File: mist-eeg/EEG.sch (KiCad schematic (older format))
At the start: 62 parts, among them J3 Electrodes, U8 ADS1299

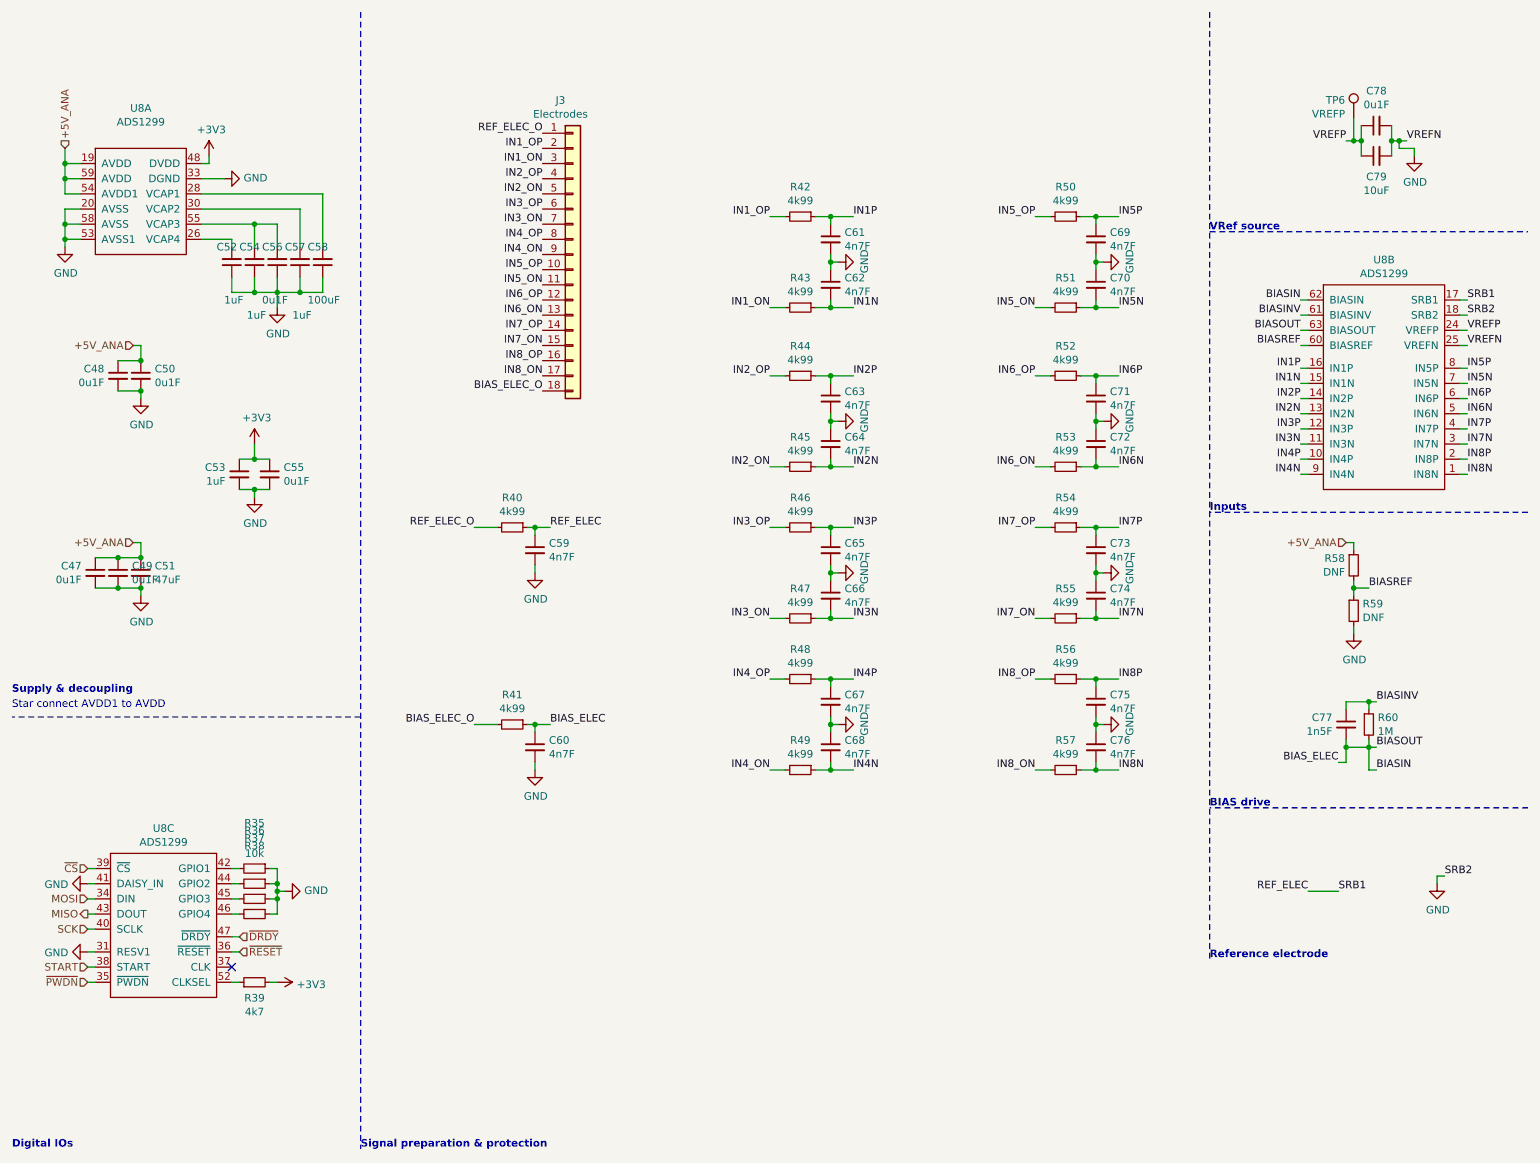
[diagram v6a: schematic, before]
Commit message: Switch to POL switching regulator to accelerate production of the board
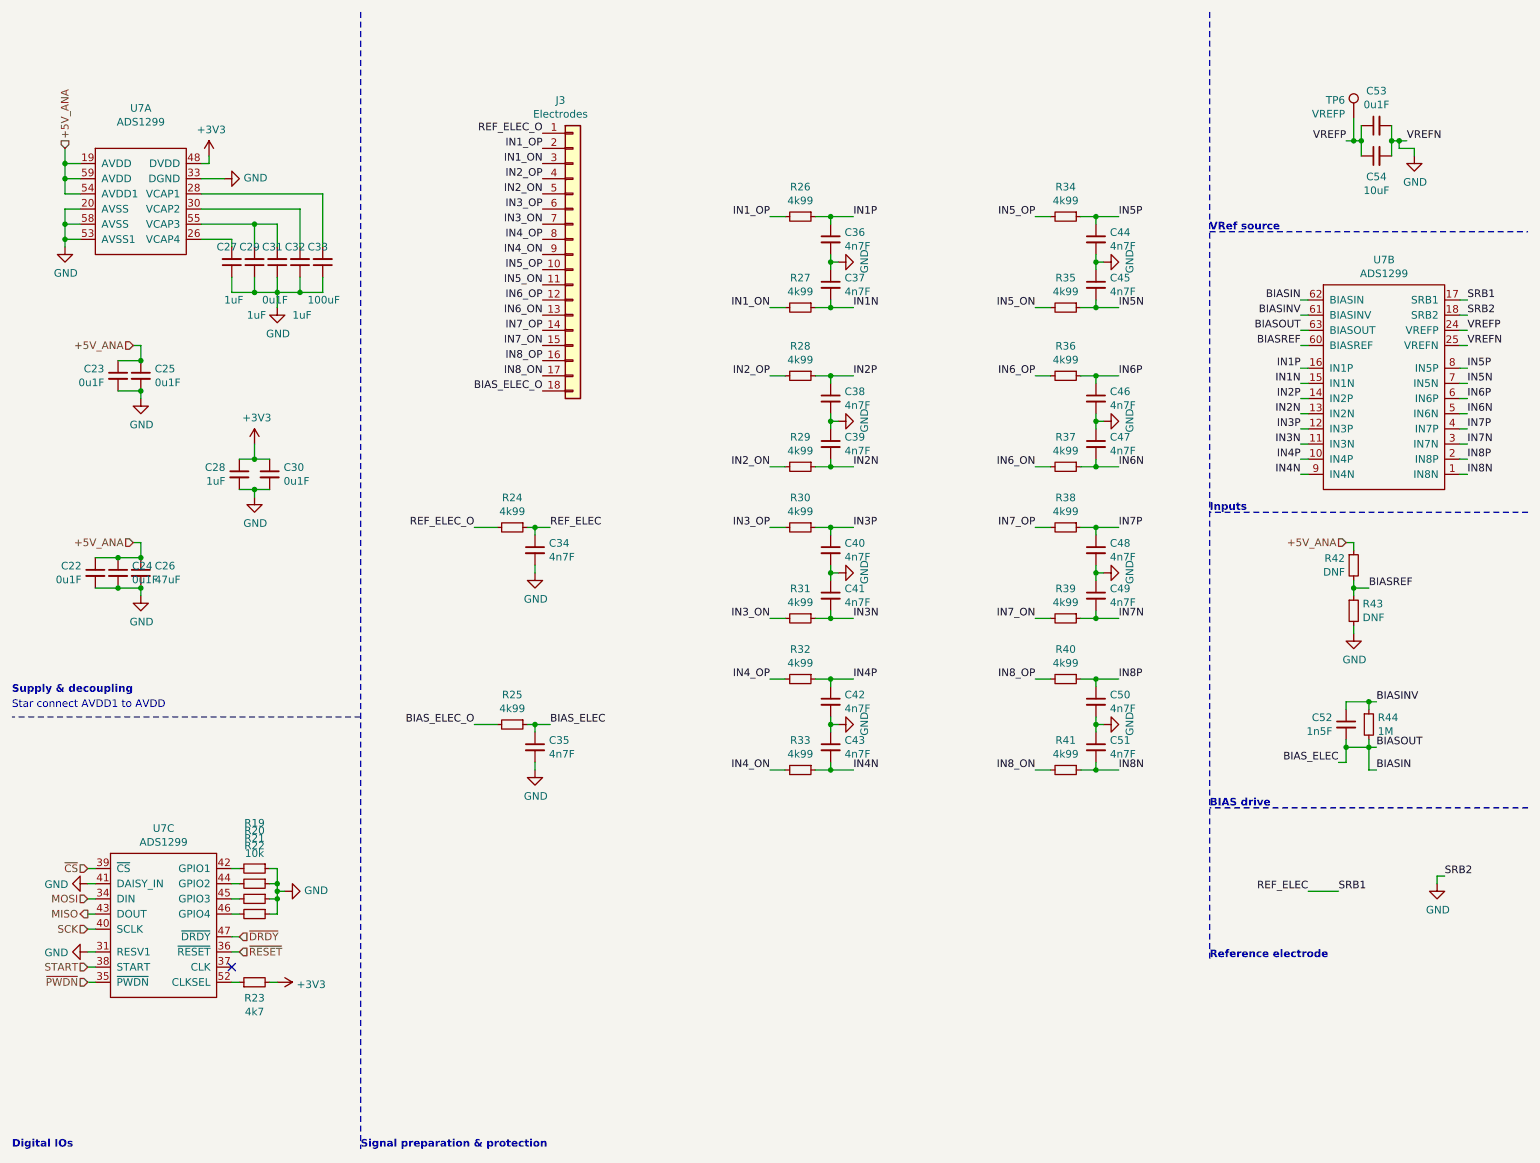
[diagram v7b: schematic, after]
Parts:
- renumbered C47 to C22, C48 to C23, C49 to C24, C50 to C25, C51 to C26, C52 to C27, C53 to C28, C54 to C29, C55 to C30, C56 to C31, C57 to C32, C58 to C33, C59 to C34, C60 to C35, C61 to C36, C62 to C37, C63 to C38, C64 to C39, C65 to C40, C66 to C41, C67 to C42, C68 to C43, C69 to C44, C70 to C45, C71 to C46, C72 to C47, C73 to C48, C74 to C49, C75 to C50, C76 to C51, C77 to C52, C78 to C53, C79 to C54, R35 to R19, R36 to R20, R37 to R21, R38 to R22, R39 to R23, R40 to R24, R41 to R25, R42 to R26, R43 to R27, R44 to R28, R45 to R29, R46 to R30, R47 to R31, R48 to R32, R49 to R33, R50 to R34, R51 to R35, R52 to R36, R53 to R37, R54 to R38, R55 to R39, R56 to R40, R57 to R41, R58 to R42, R59 to R43, R60 to R44, U8 to U7

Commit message: Add BoM
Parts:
- C26: value 47uF -> 100uF
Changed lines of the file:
@@
 P 1350 4200
 F 0 "C26" H 1442 4246 50  0000 L CNN
-F 1 "47uF" H 1442 4155 50  0000 L CNN
+F 1 "100uF" H 1442 4155 50  0000 L CNN
 F 2 "Capacitor_SMD:C_1210_3225Metric" H 1350 4200 50  0001 C CNN
 F 3 "~" H 1350 4200 50  0001 C CNN
